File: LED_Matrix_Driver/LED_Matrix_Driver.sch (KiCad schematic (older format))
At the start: 74 parts, among them J1 Screw_Terminal_01x02, J2 LED Anode Rows, J3 Columns 24-31 LED Cathodes, J4 Columns 16-23 LED Cathodes, J5 Columns 8-15 LED Cathodes, J6 Columns 0-7 LED Cathodes, SW1 OK, SW2 BACK, SW3 F1, SW4 F2, SW5 F3, SW6 F4, U1 ESP32-DEVKITC-32E, U2 74HCT244, U3 MIC2981, U4 74HC238, U5 HEF4794B, U6 HEF4794B, U7 HEF4794B, U8 HEF4794B

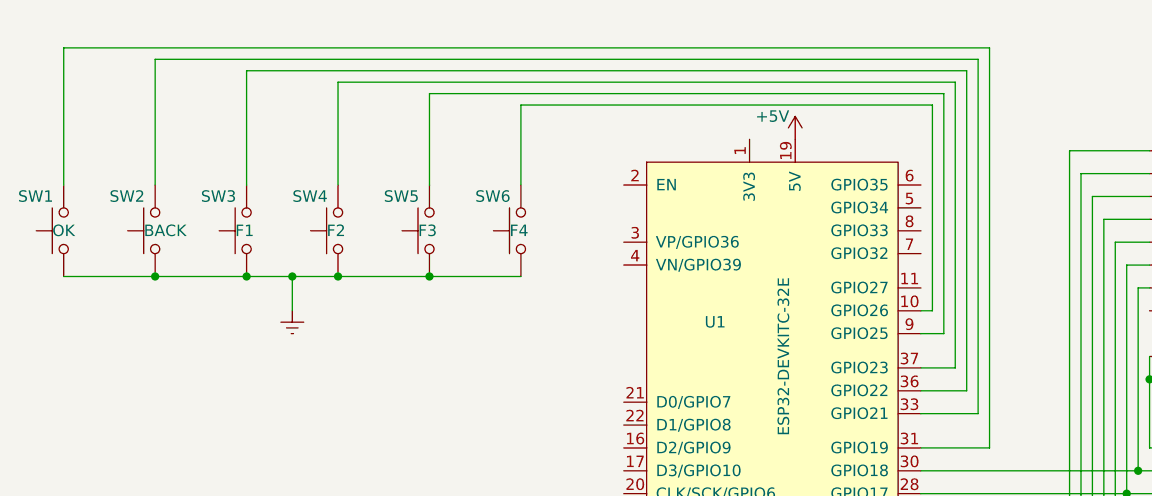
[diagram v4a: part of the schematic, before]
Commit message: Updated Driver board to include sinlge header for all 6 buttons
Created new daughter board to hold the buttons
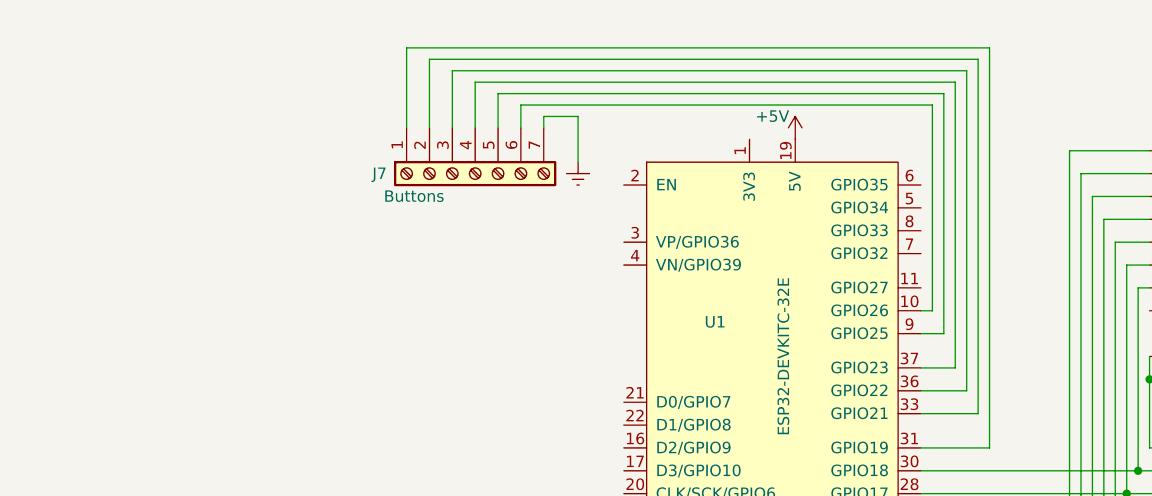
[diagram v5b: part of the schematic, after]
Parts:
- removed SW1: OK, Arduino:Custom_Pin_Header, symbol Switch:SW_Push
- removed SW2: BACK, Arduino:Custom_Pin_Header, symbol Switch:SW_Push
- removed SW3: F1, Arduino:Custom_Pin_Header, symbol Switch:SW_Push
- removed SW4: F2, Arduino:Custom_Pin_Header, symbol Switch:SW_Push
- removed SW5: F3, Arduino:Custom_Pin_Header, symbol Switch:SW_Push
- removed SW6: F4, Arduino:Custom_Pin_Header, symbol Switch:SW_Push
- added J7: Buttons, Arduino:Custom_Pin_Header, symbol Connector:Screw_Terminal_01x07
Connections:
- net Earth: now also J7.7 (Pin_7)
- net at U1.10 (GPIO26): now also J7.6 (Pin_6)
- net at U1.31 (GPIO19): now also J7.1 (Pin_1)
- net at U1.33 (GPIO21): now also J7.2 (Pin_2)
- net at U1.36 (GPIO22): now also J7.3 (Pin_3)
- net at U1.37 (GPIO23): now also J7.4 (Pin_4)
- net at U1.9 (GPIO25): now also J7.5 (Pin_5)
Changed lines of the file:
@@
 	1    0    0    -1
 $EndComp
-$Comp
-L Switch:SW_Push SW6
-U 1 1 658676FC
-P 3250 1400
-F 0 "SW6" V 3100 1600 50  0000 R CNN
-F 1 "F4" V 3250 1450 50  0000 R CNN
-F 2 "Arduino:Custom_Pin_Header" H 3250 1600 50  0001 C CNN
-F 3 "~" H 3250 1600 50  0001 C CNN
-	1    3250 1400
-	0    -1   1    0
-$EndComp
-$Comp
-L Switch:SW_Push SW5
-U 1 1 6586BF68
-P 2850 1400
-F 0 "SW5" V 2700 1600 50  0000 R CNN
-F 1 "F3" V 2850 1450 50  0000 R CNN
-F 2 "Arduino:Custom_Pin_Header" H 2850 1600 50  0001 C CNN
-F 3 "~" H 2850 1600 50  0001 C CNN
-	1    2850 1400
-	0    -1   1    0
-$EndComp
-$Comp
-L Switch:SW_Push SW4
-U 1 1 6586C49E
-P 2450 1400
-F 0 "SW4" V 2300 1600 50  0000 R CNN
-F 1 "F2" V 2450 1450 50  0000 R CNN
-F 2 "Arduino:Custom_Pin_Header" H 2450 1600 50  0001 C CNN
-F 3 "~" H 2450 1600 50  0001 C CNN
-	1    2450 1400
-	0    -1   1    0
-$EndComp
-$Comp
-L Switch:SW_Push SW3
-U 1 1 6586C73A
-P 2050 1400
-F 0 "SW3" V 1900 1600 50  0000 R CNN
-F 1 "F1" V 2050 1450 50  0000 R CNN
-F 2 "Arduino:Custom_Pin_Header" H 2050 1600 50  0001 C CNN
-F 3 "~" H 2050 1600 50  0001 C CNN
-	1    2050 1400
-	0    -1   1    0
-$EndComp
-$Comp
-L Switch:SW_Push SW2
-U 1 1 6586CCB3
-P 1650 1400
-F 0 "SW2" V 1500 1600 50  0000 R CNN
-F 1 "BACK" V 1650 1450 50  0000 R CNN
-F 2 "Arduino:Custom_Pin_Header" H 1650 1600 50  0001 C CNN
-F 3 "~" H 1650 1600 50  0001 C CNN
-	1    1650 1400
-	0    -1   1    0
-$EndComp
-$Comp
-L Switch:SW_Push SW1
-U 1 1 6590598D
-P 1250 1400
-F 0 "SW1" V 1100 1600 50  0000 R CNN
-F 1 "OK" V 1250 1450 50  0000 R CNN
-F 2 "Arduino:Custom_Pin_Header" H 1250 1600 50  0001 C CNN
-F 3 "~" H 1250 1600 50  0001 C CNN
-	1    1250 1400
-	0    -1   1    0
-$EndComp
-Wire Wire Line
-	3250 1200 3250 850
-Wire Wire Line
-	3250 850  5050 850
 Wire Wire Line
 	5050 850  5050 1750
@@
 	5050 1750 5000 1750
 Wire Wire Line
-	2850 1200 2850 800
-Wire Wire Line
-	2850 800  5100 800
-Wire Wire Line
 	5100 800  5100 1850
 Wire Wire Line
 	5100 1850 5000 1850
 Wire Wire Line
-	2450 1200 2450 750
-Wire Wire Line
-	2450 750  5150 750
-Wire Wire Line
 	5150 750  5150 2000
 Wire Wire Line
 	5150 2000 5000 2000
-Wire Wire Line
-	2050 1200 2050 700
-Wire Wire Line
-	2050 700  5200 700
 Wire Wire Line
 	5200 700  5200 2100
@@
 	5250 2200 5250 650
 Wire Wire Line
-	5250 650  1650 650
-Wire Wire Line
-	1650 650  1650 1200
-Wire Wire Line
-	1250 1200 1250 600
-Wire Wire Line
-	1250 600  5300 600
+	5250 650  2850 650
 Wire Wire Line
 	5300 600  5300 2350
 Wire Wire Line
 	5300 2350 5000 2350
-Wire Wire Line
-	1250 1600 1650 1600
-Connection ~ 2850 1600
-Wire Wire Line
-	2850 1600 3250 1600
-Connection ~ 2450 1600
-Wire Wire Line
-	2450 1600 2850 1600
-Connection ~ 1650 1600
-Wire Wire Line
-	1650 1600 2050 1600
-Wire Wire Line
-	2050 1600 2250 1600
-Connection ~ 2050 1600
-Wire Wire Line
-	2250 1600 2250 1750
-Connection ~ 2250 1600
-Wire Wire Line
-	2250 1600 2450 1600
 $Comp
 L power:Earth #PWR014
 U 1 1 65AE4D92
-P 2250 1750
-F 0 "#PWR014" H 2250 1500 50  0001 C CNN
-F 1 "Earth" H 2250 1600 50  0001 C CNN
-F 2 "" H 2250 1750 50  0001 C CNN
-F 3 "~" H 2250 1750 50  0001 C CNN
-	1    2250 1750
+P 3500 1100
+F 0 "#PWR014" H 3500 850 50  0001 C CNN
+F 1 "Earth" H 3500 950 50  0001 C CNN
+F 2 "" H 3500 1100 50  0001 C CNN
+F 3 "~" H 3500 1100 50  0001 C CNN
+	1    3500 1100
 	1    0    0    -1
 $EndComp
+$Comp
+L Connector:Screw_Terminal_01x07 J7
+U 1 1 65792D9F
+P 3050 1150
+F 0 "J7" V 3050 1600 50  0000 R CNN
+F 1 "Buttons" V 3150 1550 50  0000 R CNN
+F 2 "Arduino:Custom_Pin_Header" H 3050 1150 50  0001 C CNN
+F 3 "~" H 3050 1150 50  0001 C CNN
+	1    3050 1150
+	0    -1   1    0
+$EndComp
+Wire Wire Line
+	3500 1100 3500 900
+Wire Wire Line
+	3500 900  3350 900
+Wire Wire Line
+	3350 900  3350 950
+Wire Wire Line
+	3250 850  5050 850
+Wire Wire Line
+	3250 950  3250 850
+Wire Wire Line
+	3150 950  3150 800
+Wire Wire Line
+	3150 800  5100 800
+Wire Wire Line
+	3050 950  3050 750
+Wire Wire Line
+	3050 750  5150 750
+Wire Wire Line
+	2950 950  2950 700
+Wire Wire Line
+	2950 700  5200 700
+Wire Wire Line
+	2850 650  2850 950
+Wire Wire Line
+	2750 950  2750 600
+Wire Wire Line
+	2750 600  5300 600
 $EndSCHEMATC

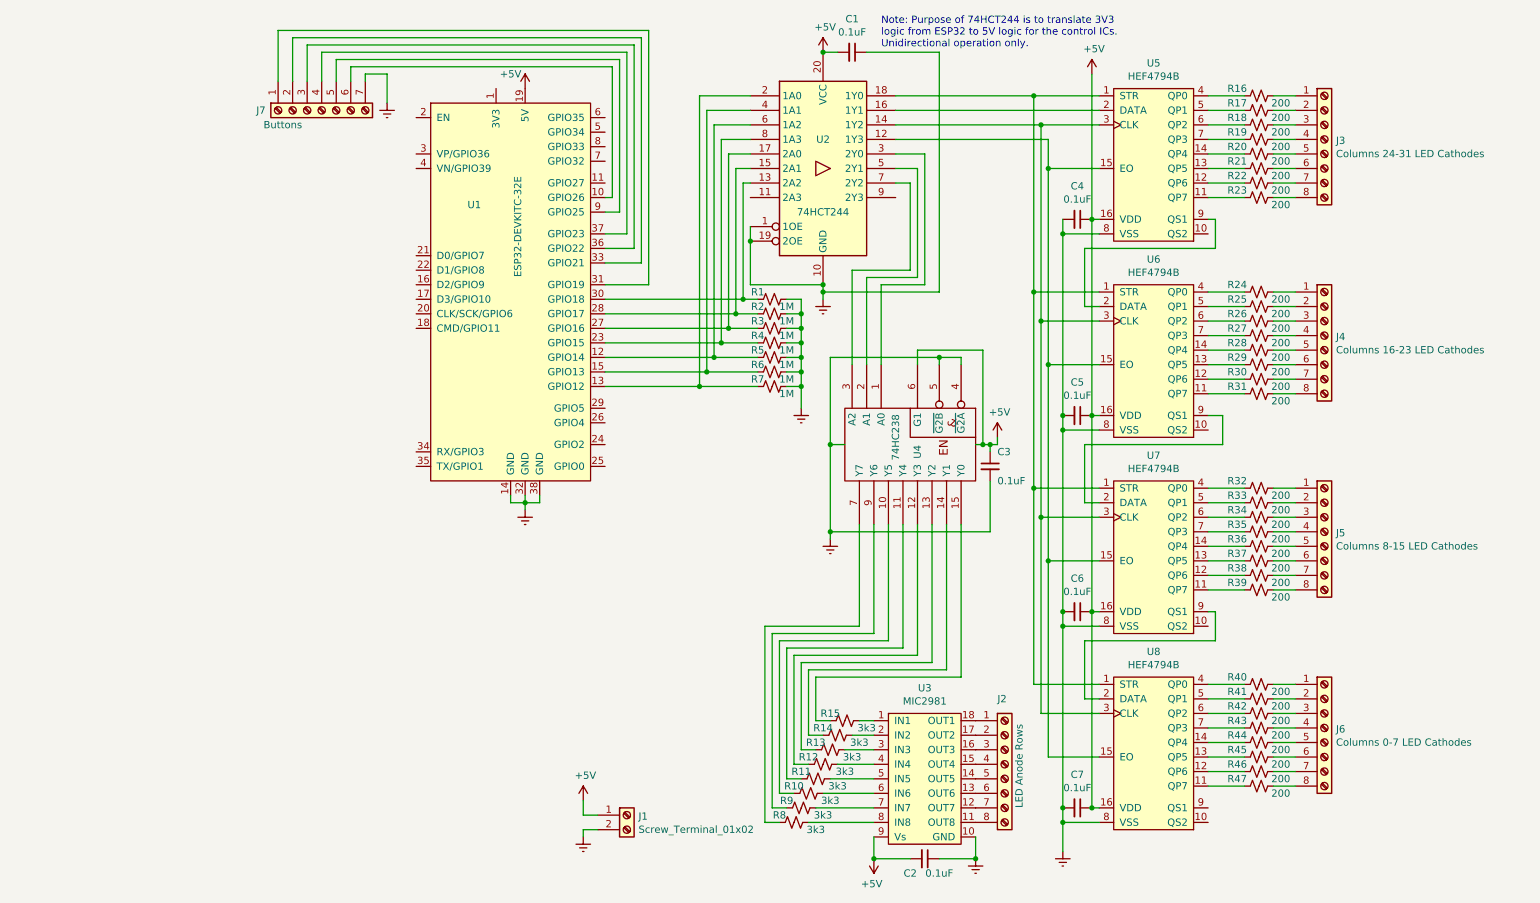
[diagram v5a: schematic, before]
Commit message: Added audio input circuitry for potential audio applications
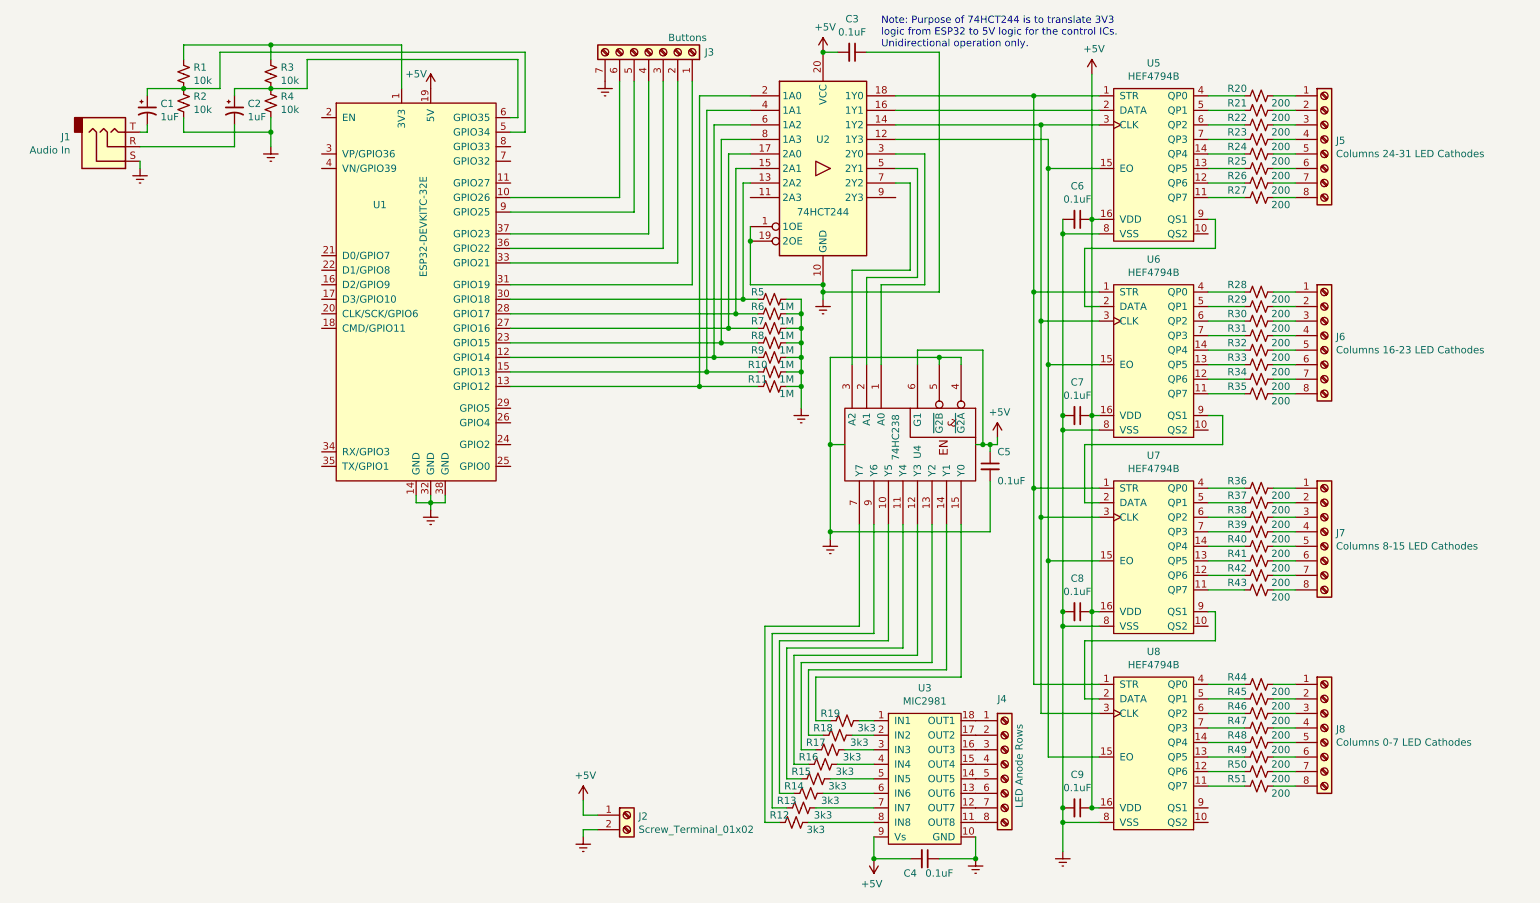
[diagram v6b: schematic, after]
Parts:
- added C1, C2: 1uF, Capacitor_THT:CP_Radial_D4.0mm_P2.00mm, symbol Device:CP1_Small
- added J1: Audio In, Arduino:Custom_Pin_Header_3, symbol Connector:AudioJack3
- added R1, R2, R3, R4: 10k, Resistor_THT:R_Axial_DIN0207_L6.3mm_D2.5mm_P10.16mm_Horizontal, symbol Device:R_Small_US
- J3: renamed from J7; footprint Arduino:Custom_Pin_Header -> Arduino:Custom_Pin_Header_7
- renumbered C1 to C3, C2 to C4, C3 to C5, C4 to C6, C5 to C7, C6 to C8, C7 to C9, J1 to J2, J2 to J4, J3 to J5, J4 to J6, J5 to J7, J6 to J8, R6 to R10, R7 to R11, R8 to R12, R9 to R13, R10 to R14, R11 to R15, R12 to R16, R13 to R17, R14 to R18, R15 to R19, R16 to R20, R17 to R21, R18 to R22, R19 to R23, R20 to R24, R21 to R25, R22 to R26, R23 to R27, R24 to R28, R25 to R29, R26 to R30, R27 to R31, R28 to R32, R29 to R33, R30 to R34, R31 to R35, R32 to R36, R33 to R37, R34 to R38, R35 to R39, R36 to R40, R37 to R41, R38 to R42, R39 to R43, R40 to R44, R41 to R45, R42 to R46, R43 to R47, R44 to R48, R45 to R49, R1 to R5, R46 to R50, R47 to R51, R2 to R6, R3 to R7, R4 to R8, R5 to R9
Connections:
- net Earth: now also J1.S, R2.1, R4.1
- net at U1.1 (3V3): now also R1.2, R3.2
- net at U1.5 (GPIO34): now also C1.1, R1.1, R2.2
- net at U1.6 (GPIO35): now also C2.1, R3.1, R4.2
- new net: C2.2, J1.R
- new net: C1.2, J1.T
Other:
- moved on the sheet: J3, U1
